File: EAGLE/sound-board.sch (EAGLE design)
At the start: 99 parts, among them IC1 SN76477, J0 POWER, J1 CON, J2 CON, J3 AUDIO, P10 1M, P2 1M, P3 1M, P4 1M, P6 50k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

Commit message: Minor modifications to PCB
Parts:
- added C27_THT: 10u, rcl:CPOL-EUE2.5-5
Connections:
- net GND: now also C27_THT.-
- net N$13: now also C27_THT.+
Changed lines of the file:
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@@
 <part name="J3" library="con-molex" library_urn="urn:adsk.eagle:library:165" deviceset="22-23-2031" device="" value="AUDIO"/>
 <part name="GND22" library="supply1" library_urn="urn:adsk.eagle:library:371" deviceset="GND" device=""/>
+<part name="C27_THT" library="rcl" library_urn="urn:adsk.eagle:library:334" deviceset="CPOL-EU" device="E2.5-5" package3d_urn="urn:adsk.eagle:package:23344/1" value="10u"/>
+<part name="GND23" library="supply1" library_urn="urn:adsk.eagle:library:371" deviceset="GND" device=""/>
 </parts>
 <sheets>
@@
 <instance part="J3" gate="-3" x="137.16" y="-17.78" rot="MR0"/>
 <instance part="GND22" gate="1" x="144.78" y="-12.7" rot="R90"/>
+<instance part="C27_THT" gate="G$1" x="116.84" y="-73.66"/>
+<instance part="GND23" gate="1" x="116.84" y="-81.28"/>
 </instances>
 <busses>
@@
 <pinref part="GND22" gate="1" pin="GND"/>
 </segment>
+<segment>
+<pinref part="C27_THT" gate="G$1" pin="-"/>
+<pinref part="GND23" gate="1" pin="GND"/>
+</segment>
 </net>
 <net name="NOISE_OSC_RES" class="0">
@@
 <pinref part="CON_SPEAKER" gate="-2" pin="S"/>
 <wire x1="106.68" y1="-66.04" x2="109.22" y2="-66.04" width="0.1524" layer="91"/>
-</segment>
-</net>
+<pinref part="C27_THT" gate="G$1" pin="+"/>
+<wire x1="116.84" y1="-71.12" x2="106.68" y2="-71.12" width="0.1524" layer="91"/>
+<junction x="106.68" y="-71.12"/>
+</segment>
+</net>

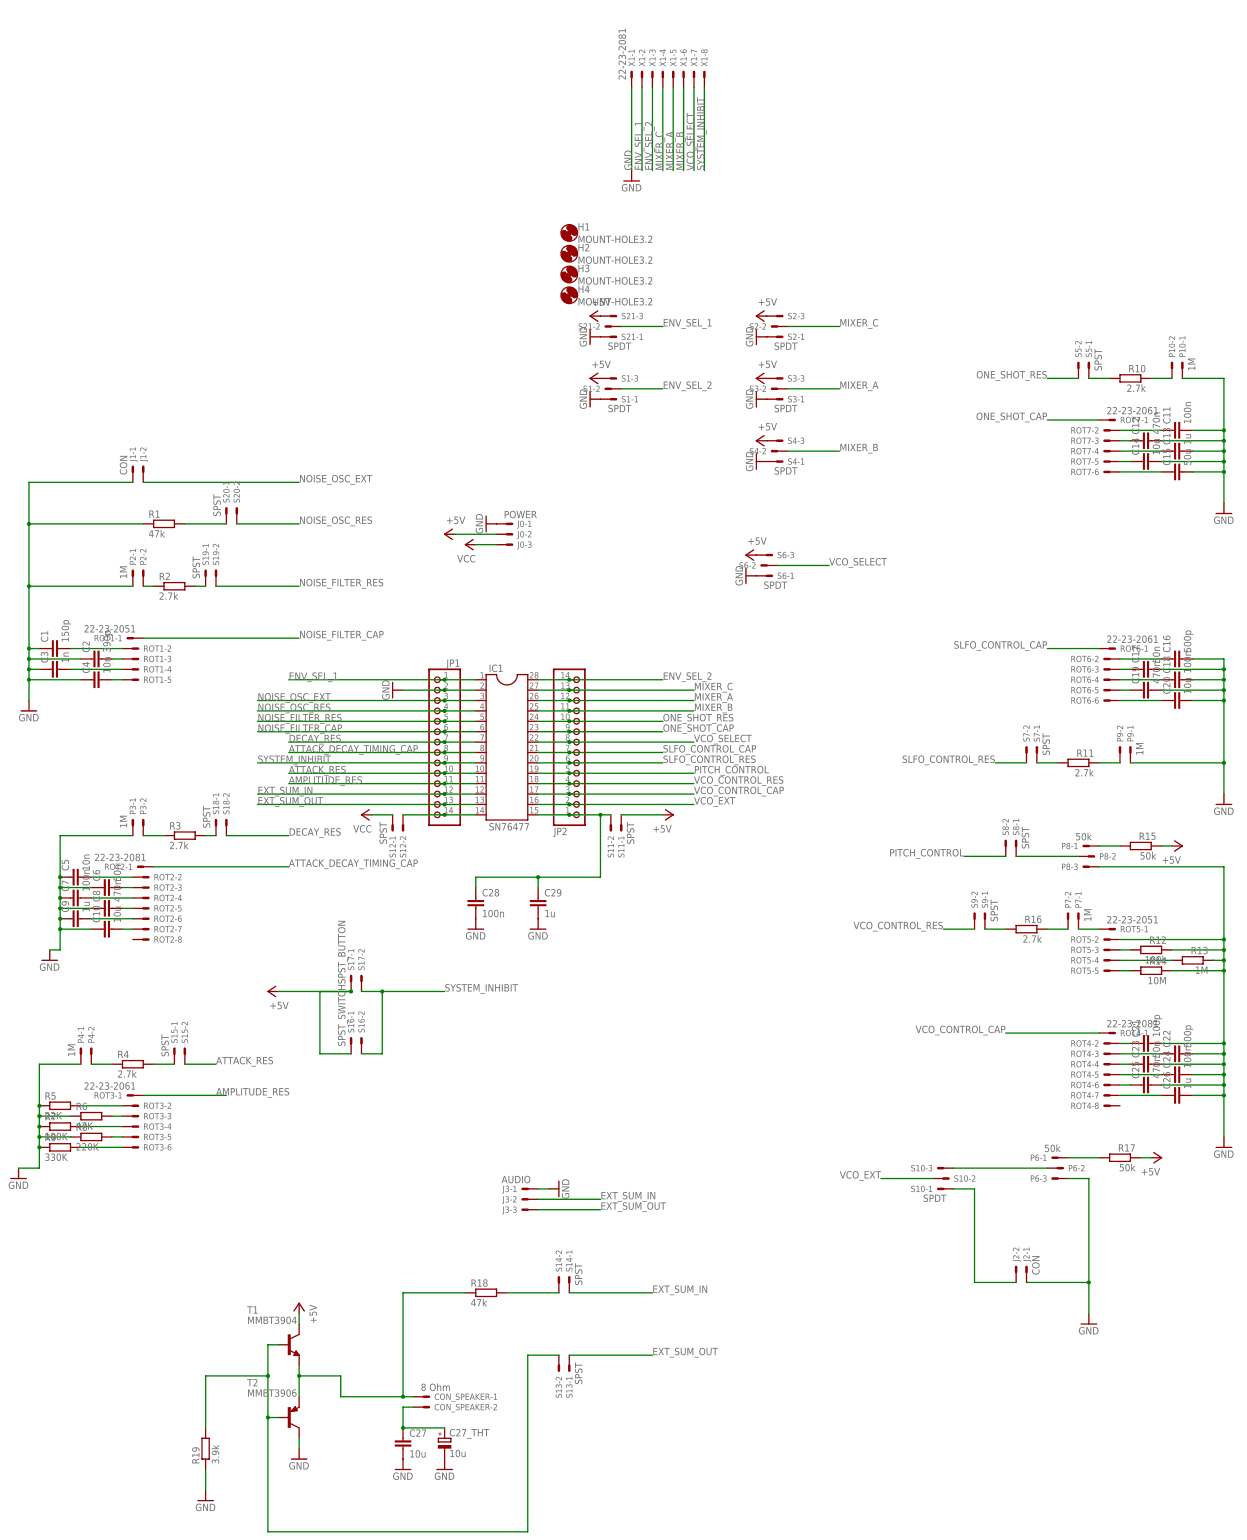
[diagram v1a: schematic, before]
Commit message: Rearrange schematic components
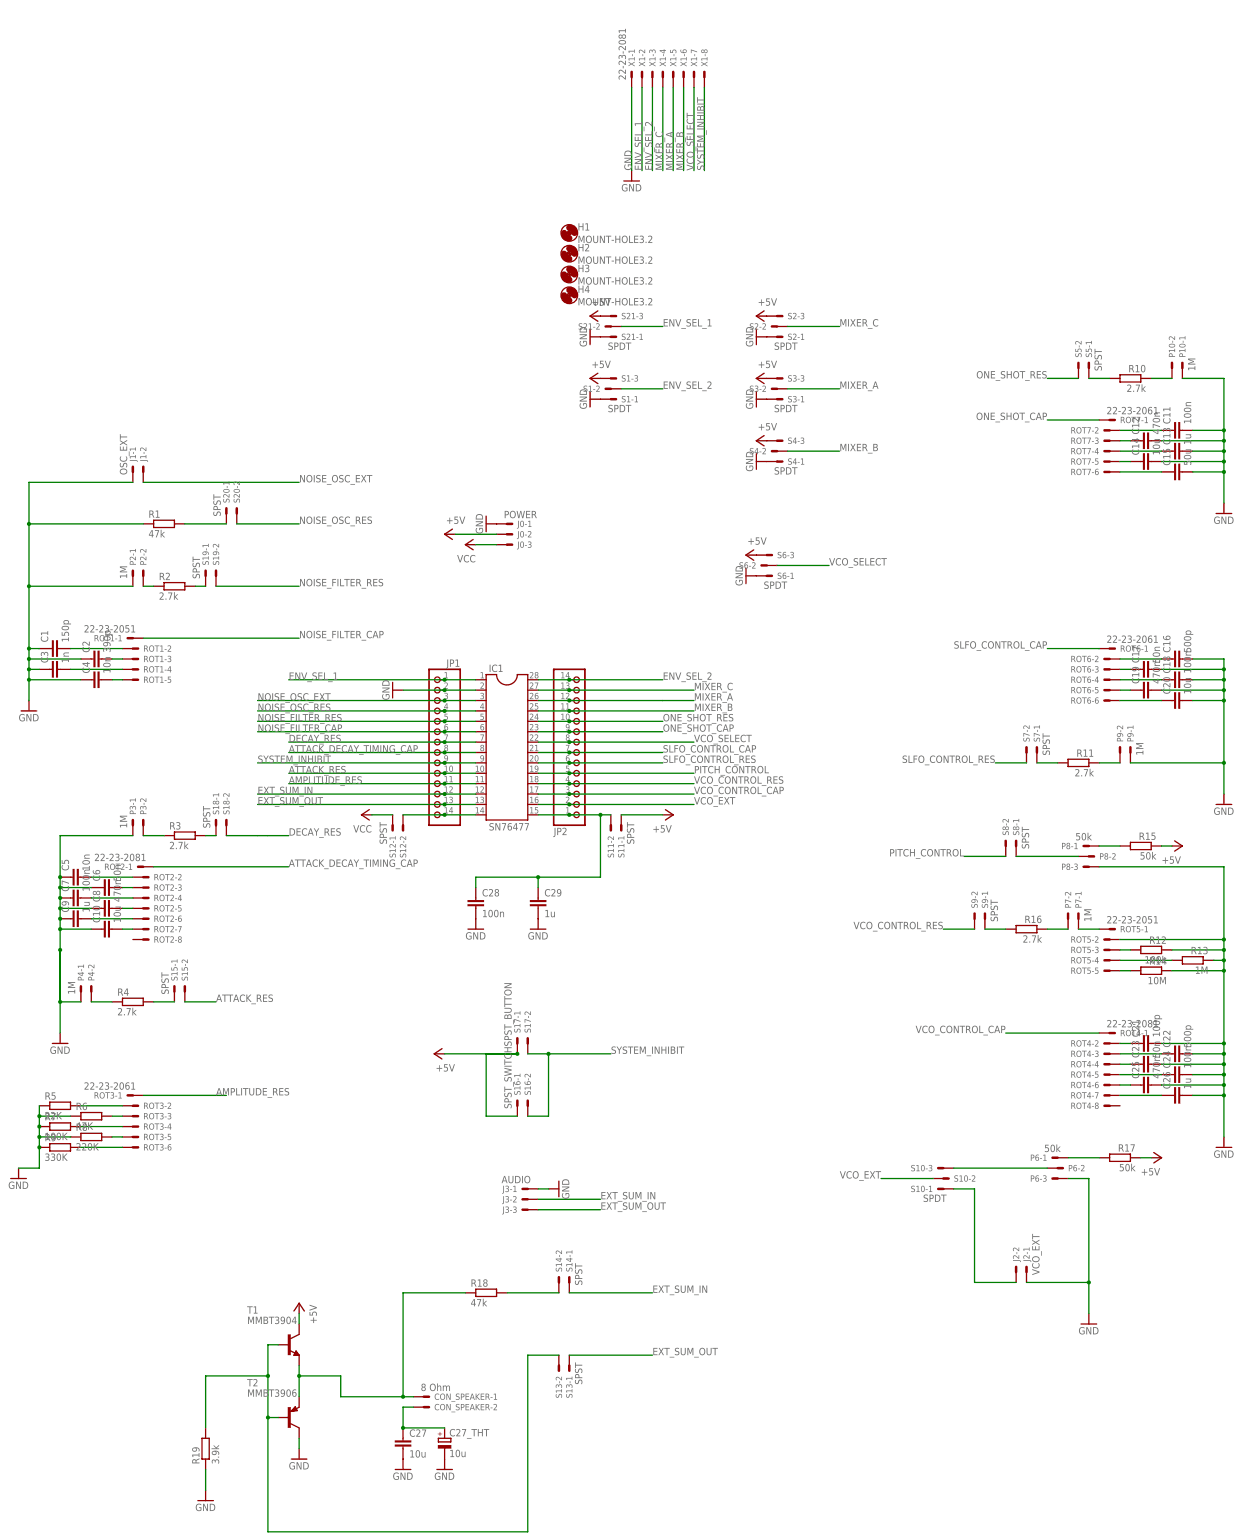
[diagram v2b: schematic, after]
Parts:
- J1: value CON -> OSC_EXT
- J2: value CON -> VCO_EXT
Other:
- moved on the sheet: P4-1, P4-2, R4, S15-1, S15-2, S16-1, S16-2, S17-1, S17-2
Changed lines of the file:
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@@
 <part name="C9" library="rcl" library_urn="urn:adsk.eagle:library:334" deviceset="C-EU" device="C0805" package3d_urn="urn:adsk.eagle:package:23617/2" value="1u"/>
 <part name="C10" library="rcl" library_urn="urn:adsk.eagle:library:334" deviceset="C-EU" device="C0805" package3d_urn="urn:adsk.eagle:package:23617/2" value="10u"/>
-<part name="J1" library="con-molex" library_urn="urn:adsk.eagle:library:165" deviceset="22-23-2021" device="" value="CON"/>
+<part name="J1" library="con-molex" library_urn="urn:adsk.eagle:library:165" deviceset="22-23-2021" device="" value="OSC_EXT"/>
 <part name="S17" library="con-molex" library_urn="urn:adsk.eagle:library:165" deviceset="22-23-2021" device="" value="SPST_BUTTON"/>
 <part name="S16" library="con-molex" library_urn="urn:adsk.eagle:library:165" deviceset="22-23-2021" device="" value="SPST_SWITCH"/>
@@
 <part name="GND13" library="supply1" library_urn="urn:adsk.eagle:library:371" deviceset="GND" device=""/>
 <part name="S10" library="con-molex" library_urn="urn:adsk.eagle:library:165" deviceset="22-23-2031" device="" value="SPDT"/>
-<part name="J2" library="con-molex" library_urn="urn:adsk.eagle:library:165" deviceset="22-23-2021" device="" value="CON"/>
+<part name="J2" library="con-molex" library_urn="urn:adsk.eagle:library:165" deviceset="22-23-2021" device="" value="VCO_EXT"/>
 <part name="P6" library="con-molex" library_urn="urn:adsk.eagle:library:165" deviceset="22-23-2031" device="" value="50k"/>
 <part name="R17" library="rcl" library_urn="urn:adsk.eagle:library:334" deviceset="R-EU_" device="R0805" package3d_urn="urn:adsk.eagle:package:23553/2" value="50k"/>
@@
 <instance part="P3" gate="-1" x="40.64" y="76.2" rot="R90"/>
 <instance part="P3" gate="-2" x="43.18" y="76.2" rot="R90"/>
-<instance part="GND1" gate="1" x="20.32" y="43.18"/>
+<instance part="GND1" gate="1" x="22.86" y="22.86"/>
 <instance part="R3" gate="G$1" x="53.34" y="73.66"/>
 <instance part="ROT2" gate="-1" x="43.18" y="66.04" rot="MR0"/>
@@
 <instance part="J1" gate="-1" x="40.64" y="162.56" rot="R90"/>
 <instance part="J1" gate="-2" x="43.18" y="162.56" rot="R90"/>
-<instance part="S17" gate="-1" x="93.98" y="38.1" rot="R90"/>
-<instance part="S17" gate="-2" x="96.52" y="38.1" rot="R90"/>
-<instance part="S16" gate="-1" x="93.98" y="22.86" rot="R90"/>
-<instance part="S16" gate="-2" x="96.52" y="22.86" rot="R90"/>
-<instance part="P+1" gate="1" x="73.66" y="35.56" rot="R90"/>
+<instance part="S17" gate="-1" x="134.62" y="22.86" rot="R90"/>
+<instance part="S17" gate="-2" x="137.16" y="22.86" rot="R90"/>
+<instance part="S16" gate="-1" x="134.62" y="7.62" rot="R90"/>
+<instance part="S16" gate="-2" x="137.16" y="7.62" rot="R90"/>
+<instance part="P+1" gate="1" x="114.3" y="20.32" rot="R90"/>
 <instance part="S18" gate="-1" x="60.96" y="76.2" rot="R90"/>
 <instance part="S18" gate="-2" x="63.5" y="76.2" rot="R90"/>
@@
 <instance part="ROT3" gate="-5" x="40.64" y="0"/>
 <instance part="ROT3" gate="-6" x="40.64" y="-2.54"/>
-<instance part="P4" gate="-1" x="27.94" y="20.32" rot="R90"/>
-<instance part="P4" gate="-2" x="30.48" y="20.32" rot="R90"/>
-<instance part="R4" gate="G$1" x="40.64" y="17.78"/>
-<instance part="S15" gate="-1" x="50.8" y="20.32" rot="R90"/>
-<instance part="S15" gate="-2" x="53.34" y="20.32" rot="R90"/>
+<instance part="P4" gate="-1" x="27.94" y="35.56" rot="R90"/>
+<instance part="P4" gate="-2" x="30.48" y="35.56" rot="R90"/>
+<instance part="R4" gate="G$1" x="40.64" y="33.02"/>
+<instance part="S15" gate="-1" x="50.8" y="35.56" rot="R90"/>
+<instance part="S15" gate="-2" x="53.34" y="35.56" rot="R90"/>
 <instance part="GND4" gate="1" x="12.7" y="-10.16"/>
 <instance part="R5" gate="G$1" x="22.86" y="7.62"/>
@@
 </segment>
 <segment>
+<pinref part="R9" gate="G$1" pin="1"/>
+<junction x="17.78" y="-2.54"/>
+<pinref part="R5" gate="G$1" pin="1"/>
+<wire x1="17.78" y1="5.08" x2="17.78" y2="7.62" width="0.1524" layer="91"/>
+<pinref part="R6" gate="G$1" pin="1"/>
+<wire x1="25.4" y1="5.08" x2="17.78" y2="5.08" width="0.1524" layer="91"/>
+<junction x="17.78" y="5.08"/>
+<wire x1="17.78" y1="2.54" x2="17.78" y2="5.08" width="0.1524" layer="91"/>
+<pinref part="R7" gate="G$1" pin="1"/>
+<junction x="17.78" y="2.54"/>
+<wire x1="17.78" y1="2.54" x2="17.78" y2="0" width="0.1524" layer="91"/>
+<pinref part="R8" gate="G$1" pin="1"/>
+<wire x1="25.4" y1="0" x2="17.78" y2="0" width="0.1524" layer="91"/>
+<junction x="17.78" y="0"/>
+<wire x1="17.78" y1="0" x2="17.78" y2="-2.54" width="0.1524" layer="91"/>
+<wire x1="17.78" y1="-7.62" x2="17.78" y2="-2.54" width="0.1524" layer="91"/>
+<pinref part="GND4" gate="1" pin="GND"/>
+<wire x1="12.7" y1="-7.62" x2="17.78" y2="-7.62" width="0.1524" layer="91"/>
+</segment>
+<segment>
 <pinref part="C5" gate="G$1" pin="1"/>
 <wire x1="22.86" y1="63.5" x2="22.86" y2="60.96" width="0.1524" layer="91"/>
@@
 <wire x1="22.86" y1="53.34" x2="22.86" y2="50.8" width="0.1524" layer="91"/>
 <wire x1="22.86" y1="50.8" x2="22.86" y2="45.72" width="0.1524" layer="91"/>
-<wire x1="22.86" y1="45.72" x2="20.32" y2="45.72" width="0.1524" layer="91"/>
+<wire x1="22.86" y1="45.72" x2="22.86" y2="33.02" width="0.1524" layer="91"/>
 <pinref part="C6" gate="G$1" pin="1"/>
+<wire x1="22.86" y1="33.02" x2="22.86" y2="25.4" width="0.1524" layer="91"/>
 <wire x1="30.48" y1="60.96" x2="22.86" y2="60.96" width="0.1524" layer="91"/>
 <junction x="22.86" y="60.96"/>
@@
 <pinref part="C9" gate="G$1" pin="1"/>
 <junction x="22.86" y="53.34"/>
-</segment>
-<segment>
-<pinref part="GND4" gate="1" pin="GND"/>
-<pinref part="R5" gate="G$1" pin="1"/>
-<wire x1="12.7" y1="-7.62" x2="17.78" y2="-7.62" width="0.1524" layer="91"/>
-<wire x1="17.78" y1="-7.62" x2="17.78" y2="-2.54" width="0.1524" layer="91"/>
-<pinref part="R9" gate="G$1" pin="1"/>
-<wire x1="17.78" y1="2.54" x2="17.78" y2="0" width="0.1524" layer="91"/>
-<junction x="17.78" y="-2.54"/>
-<wire x1="17.78" y1="0" x2="17.78" y2="-2.54" width="0.1524" layer="91"/>
-<wire x1="17.78" y1="2.54" x2="17.78" y2="5.08" width="0.1524" layer="91"/>
-<pinref part="R7" gate="G$1" pin="1"/>
-<junction x="17.78" y="2.54"/>
-<pinref part="R6" gate="G$1" pin="1"/>
-<wire x1="17.78" y1="5.08" x2="17.78" y2="7.62" width="0.1524" layer="91"/>
-<wire x1="25.4" y1="5.08" x2="17.78" y2="5.08" width="0.1524" layer="91"/>
-<junction x="17.78" y="5.08"/>
-<pinref part="R8" gate="G$1" pin="1"/>
-<wire x1="25.4" y1="0" x2="17.78" y2="0" width="0.1524" layer="91"/>
-<junction x="17.78" y="0"/>
-<wire x1="17.78" y1="7.62" x2="17.78" y2="17.78" width="0.1524" layer="91"/>
-<junction x="17.78" y="7.62"/>
 <pinref part="P4" gate="-1" pin="S"/>
-<wire x1="17.78" y1="17.78" x2="27.94" y2="17.78" width="0.1524" layer="91"/>
+<wire x1="22.86" y1="33.02" x2="27.94" y2="33.02" width="0.1524" layer="91"/>
+<wire x1="22.86" y1="45.72" x2="22.86" y2="33.02" width="0.1524" layer="91"/>
+<junction x="22.86" y="45.72"/>
+<junction x="22.86" y="33.02"/>
 </segment>
 <segment>
@@
 <segment>
 <pinref part="S17" gate="-2" pin="S"/>
-<wire x1="96.52" y1="35.56" x2="101.6" y2="35.56" width="0.1524" layer="91"/>
-<wire x1="116.84" y1="35.56" x2="101.6" y2="35.56" width="0.1524" layer="91"/>
+<wire x1="137.16" y1="20.32" x2="142.24" y2="20.32" width="0.1524" layer="91"/>
+<wire x1="157.48" y1="20.32" x2="142.24" y2="20.32" width="0.1524" layer="91"/>
 <pinref part="S16" gate="-2" pin="S"/>
-<wire x1="96.52" y1="20.32" x2="101.6" y2="20.32" width="0.1524" layer="91"/>
-<wire x1="101.6" y1="20.32" x2="101.6" y2="35.56" width="0.1524" layer="91"/>
-<junction x="101.6" y="35.56"/>
-<label x="116.84" y="35.56" size="1.778" layer="95"/>
+<wire x1="137.16" y1="5.08" x2="142.24" y2="5.08" width="0.1524" layer="91"/>
+<wire x1="142.24" y1="5.08" x2="142.24" y2="20.32" width="0.1524" layer="91"/>
+<junction x="142.24" y="20.32"/>
+<label x="157.48" y="20.32" size="1.778" layer="95"/>
 </segment>
 <segment>
@@
 <segment>
 <pinref part="S16" gate="-1" pin="S"/>
-<wire x1="93.98" y1="20.32" x2="86.36" y2="20.32" width="0.1524" layer="91"/>
-<wire x1="86.36" y1="20.32" x2="86.36" y2="35.56" width="0.1524" layer="91"/>
+<wire x1="134.62" y1="5.08" x2="127" y2="5.08" width="0.1524" layer="91"/>
+<wire x1="127" y1="5.08" x2="127" y2="20.32" width="0.1524" layer="91"/>
 <pinref part="S17" gate="-1" pin="S"/>
-<wire x1="86.36" y1="35.56" x2="93.98" y2="35.56" width="0.1524" layer="91"/>
-<wire x1="93.98" y1="35.56" x2="76.2" y2="35.56" width="0.1524" layer="91"/>
-<junction x="93.98" y="35.56"/>
+<wire x1="127" y1="20.32" x2="134.62" y2="20.32" width="0.1524" layer="91"/>
+<wire x1="134.62" y1="20.32" x2="116.84" y2="20.32" width="0.1524" layer="91"/>
+<junction x="134.62" y="20.32"/>
 <pinref part="P+1" gate="1" pin="+5V"/>
 </segment>
@@
 <pinref part="P4" gate="-2" pin="S"/>
 <pinref part="R4" gate="G$1" pin="1"/>
-<wire x1="30.48" y1="17.78" x2="35.56" y2="17.78" width="0.1524" layer="91"/>
+<wire x1="30.48" y1="33.02" x2="35.56" y2="33.02" width="0.1524" layer="91"/>
 </segment>
 </net>
@@
 <pinref part="R4" gate="G$1" pin="2"/>
 <pinref part="S15" gate="-1" pin="S"/>
-<wire x1="45.72" y1="17.78" x2="50.8" y2="17.78" width="0.1524" layer="91"/>
+<wire x1="45.72" y1="33.02" x2="50.8" y2="33.02" width="0.1524" layer="91"/>
 </segment>
 </net>
@@
 <segment>
 <pinref part="S15" gate="-2" pin="S"/>
-<wire x1="53.34" y1="17.78" x2="60.96" y2="17.78" width="0.1524" layer="91"/>
-<label x="60.96" y="17.78" size="1.778" layer="95"/>
-</segment>
-<segment>
+<wire x1="53.34" y1="33.02" x2="60.96" y2="33.02" width="0.1524" layer="91"/>
+<label x="60.96" y="33.02" size="1.778" layer="95"/>
+</segment>
+<segment>
